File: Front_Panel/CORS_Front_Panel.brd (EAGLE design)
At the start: 158.6 x 41 mm, 19 parts

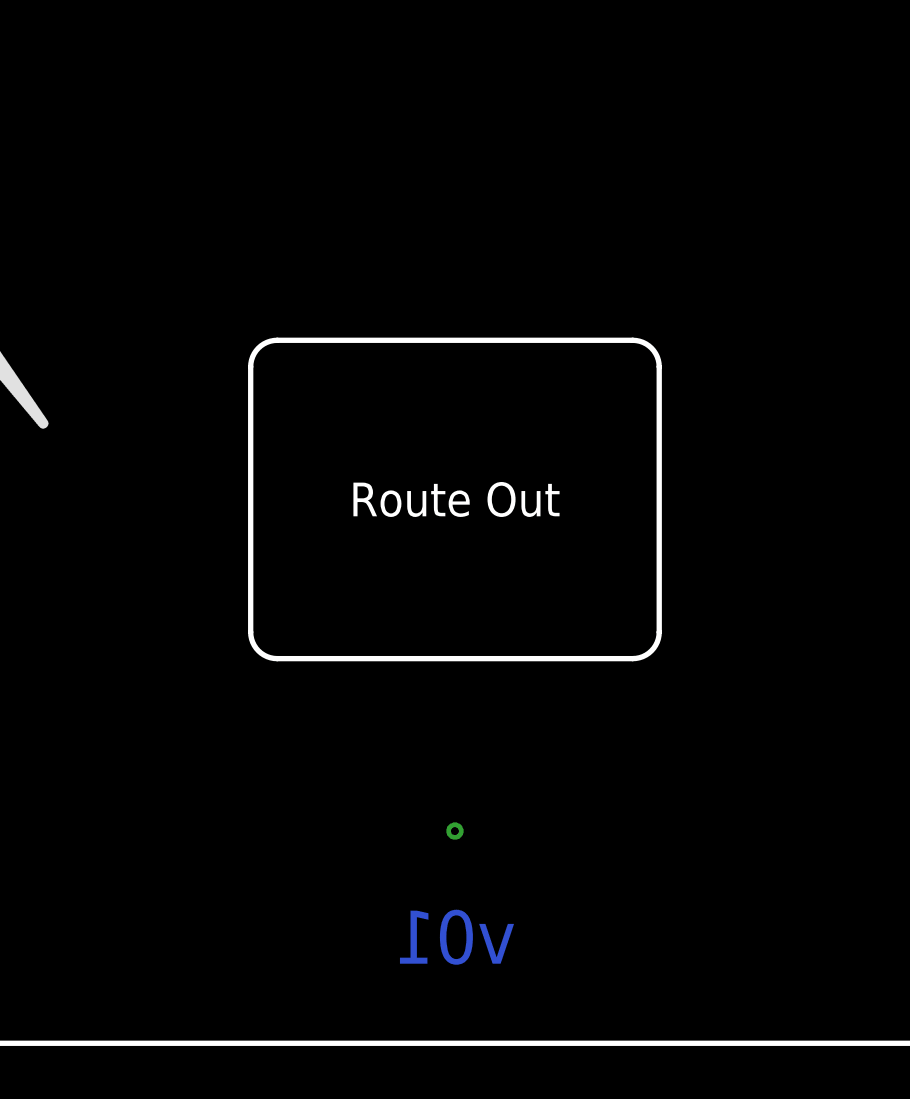
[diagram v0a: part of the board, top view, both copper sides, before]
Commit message: Update OLED and Ethernet
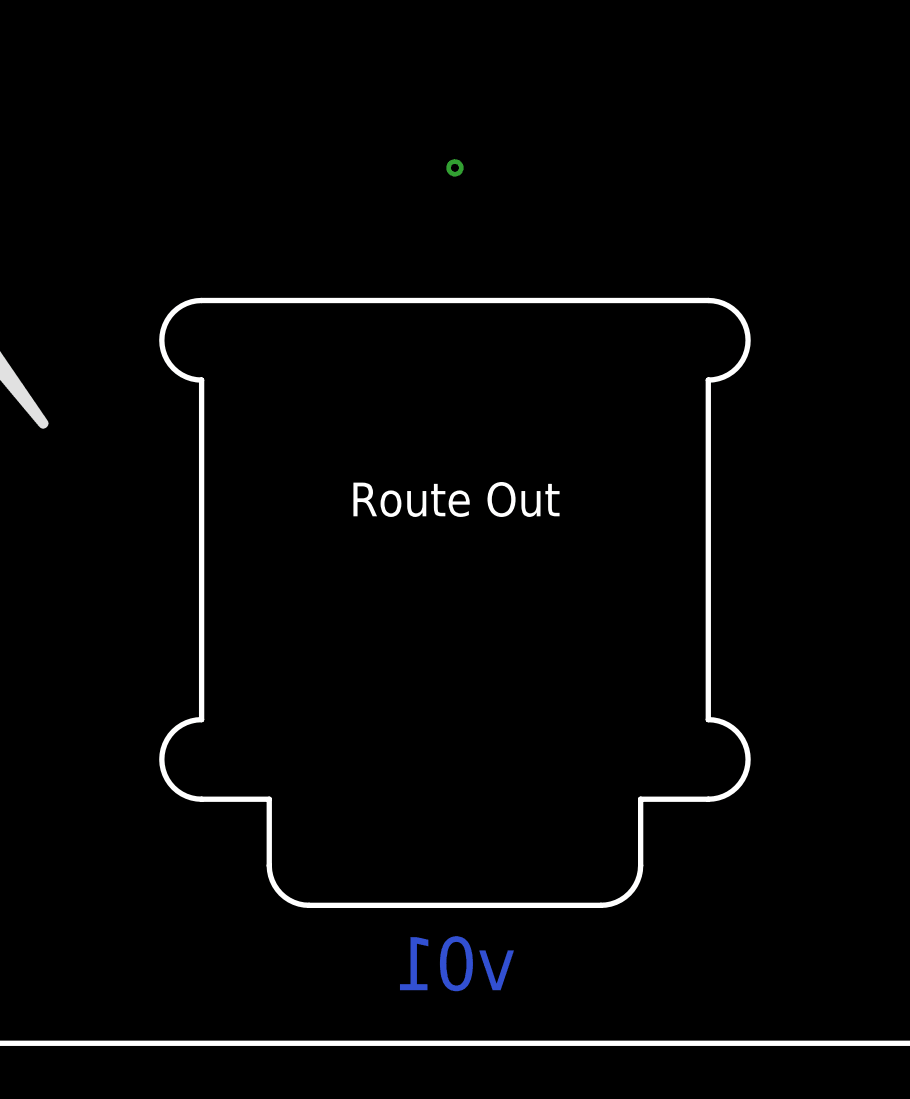
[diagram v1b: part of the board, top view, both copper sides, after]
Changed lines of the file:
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@@
 <drawing>
 <settings>
-<setting alwaysvectorfont="yes"/>
+<setting alwaysvectorfont="no"/>
 <setting verticaltext="up"/>
 </settings>
@@
 <wire x1="-75.55" y1="0.75" x2="-78.3" y2="3.5" width="0.5" layer="51" curve="-90"/>
 <wire x1="-67.8" y1="-7" x2="-70.55" y2="-4.25" width="0.5" layer="51" curve="-90"/>
-<text x="0" y="-5" size="2" layer="16" font="vector" ratio="15" rot="MR0" align="bottom-center">v01</text>
+<text x="0" y="-6" size="2" layer="16" font="vector" ratio="15" rot="MR0" align="bottom-center">v01</text>
 </plain>
 <attributes>
@@
 <vertex x="-79.3" y="-8"/>
 </polygon>
-<via x="0" y="0" extent="1-16" drill="0.3"/>
+<via x="0" y="25" extent="1-16" drill="0.3"/>
 </signal>
 </signals>

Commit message: Update panels
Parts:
- removed MICROSD: (no value), output:MICROSD0
- removed RESET_LABEL: (no value), output:RESET0
- removed U$2: (no value), output:BOOT0
- removed U$3, U$4: (no value), output:CONFIG0
- removed U$5: (no value), output:ESP320
- removed U$6: (no value), output:UBLOX0
- added U$10, U$9: (no value), output:CONFIG3
- added U$11: (no value), output:ESP324
- added U$12: (no value), output:BOOT325
- added U$13: (no value), output:UBLOX326
- added U$7: (no value), output:MICROSD1
- added U$8: (no value), output:RESET2
- moved STATUS 1.00 mm to (-63.5, 8.00)
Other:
- board text added: "v02"
- board text removed: "v01"
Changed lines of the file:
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@@
 <wire x1="-75.55" y1="0.75" x2="-78.3" y2="3.5" width="0.5" layer="51" curve="-90"/>
 <wire x1="-67.8" y1="-7" x2="-70.55" y2="-4.25" width="0.5" layer="51" curve="-90"/>
-<text x="0" y="-6" size="2" layer="16" font="vector" ratio="15" rot="MR0" align="bottom-center">v01</text>
+<text x="0" y="-6" size="2" layer="16" font="vector" ratio="15" rot="MR0" align="bottom-center">v02</text>
 </plain>
 <attributes>
@@
 <element name="LOGO1" library="SparkFun-Aesthetics" package="SFE_LOGO_NAME_FLAME_.3" value="SFE_LOGO_NAME_FLAME.3_INCH" x="-46.8504" y="17.0889" smashed="yes"/>
 <element name="U$1" library="output" package="REFERENCE_STATION0" value="" x="44" y="18" smashed="yes"/>
-<element name="STATUS" library="output" package="STATUS0" value="" x="-63.5" y="7" smashed="yes"/>
-<element name="MICROSD" library="output" package="MICROSD0" value="" x="-38.1" y="3.6" smashed="yes"/>
-<element name="RESET_LABEL" library="output" package="RESET0" value="" x="25.4" y="7" smashed="yes"/>
-<element name="U$2" library="output" package="BOOT0" value="" x="50.8" y="7" smashed="yes"/>
-<element name="U$3" library="output" package="CONFIG0" value="" x="38.1" y="6.2" smashed="yes"/>
-<element name="U$4" library="output" package="CONFIG0" value="" x="63.5" y="6.2" smashed="yes"/>
-<element name="U$5" library="output" package="ESP320" value="" x="38.1" y="4.8" smashed="yes"/>
-<element name="U$6" library="output" package="UBLOX0" value="" x="63.5" y="4.8" smashed="yes"/>
+<element name="STATUS" library="output" package="STATUS0" value="" x="-63.5" y="8" smashed="yes"/>
+<element name="U$7" library="output" package="MICROSD1" value="" x="-38.1" y="4.6" smashed="yes"/>
+<element name="U$8" library="output" package="RESET2" value="" x="25.4" y="8" smashed="yes"/>
+<element name="U$9" library="output" package="CONFIG3" value="" x="38.1" y="7.6" smashed="yes"/>
+<element name="U$10" library="output" package="CONFIG3" value="" x="63.5" y="7.6" smashed="yes"/>
+<element name="U$11" library="output" package="ESP324" value="" x="38.1" y="5.6" smashed="yes"/>
+<element name="U$12" library="output" package="BOOT325" value="" x="50.8" y="8" smashed="yes"/>
+<element name="U$13" library="output" package="UBLOX326" value="" x="63.5" y="5.6" smashed="yes"/>
 </elements>
 <signals>

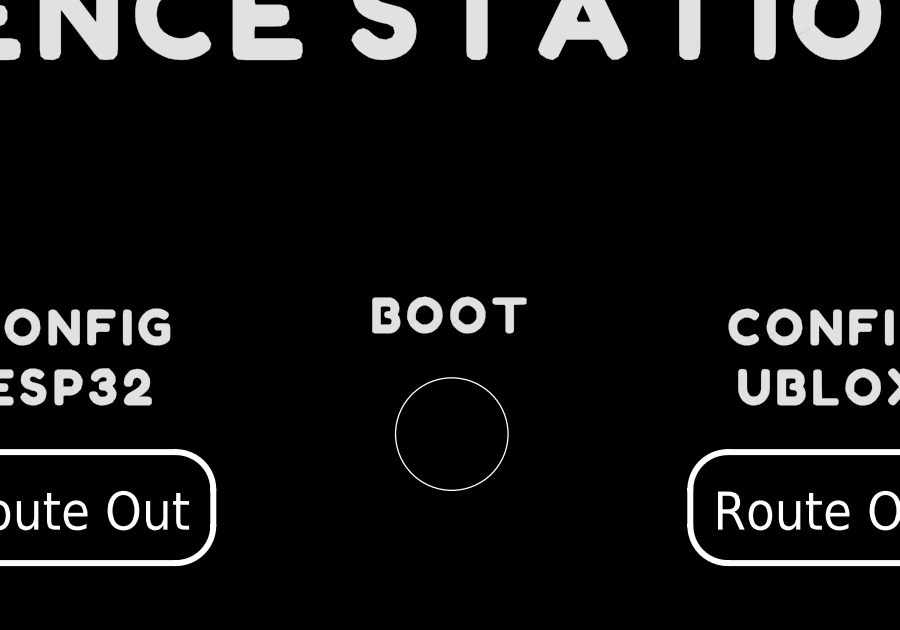
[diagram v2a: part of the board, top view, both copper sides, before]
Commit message: Move BOOT / MODE button further out. Update panels and stickers
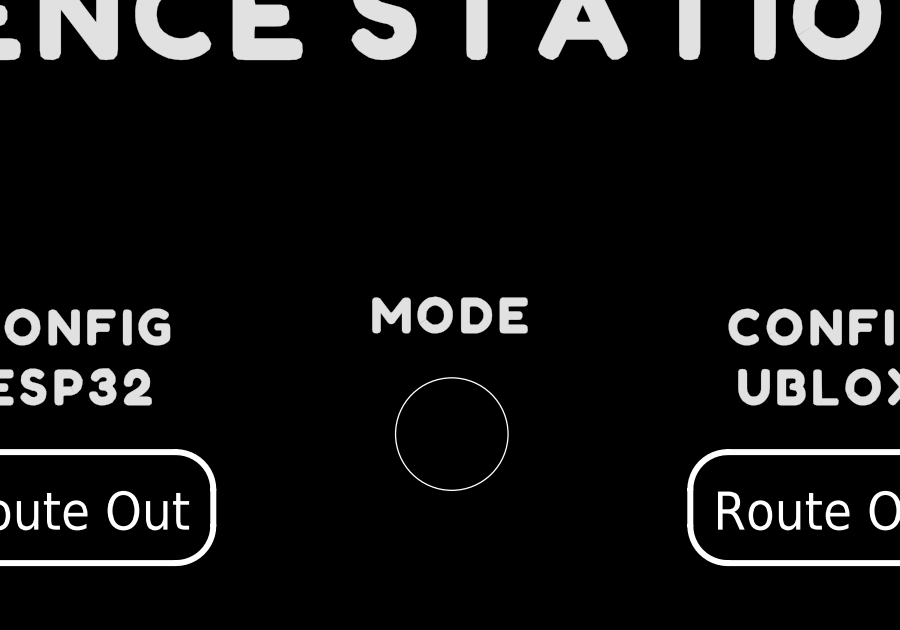
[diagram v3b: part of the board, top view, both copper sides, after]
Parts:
- removed U$12: (no value), output:BOOT325
- added U$2: (no value), output:MODE0
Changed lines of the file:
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@@
 <element name="U$10" library="output" package="CONFIG3" value="" x="63.5" y="7.6" smashed="yes"/>
 <element name="U$11" library="output" package="ESP324" value="" x="38.1" y="5.6" smashed="yes"/>
-<element name="U$12" library="output" package="BOOT325" value="" x="50.8" y="8" smashed="yes"/>
 <element name="U$13" library="output" package="UBLOX326" value="" x="63.5" y="5.6" smashed="yes"/>
+<element name="U$2" library="output" package="MODE0" value="" x="50.8" y="8" smashed="yes"/>
 </elements>
 <signals>
